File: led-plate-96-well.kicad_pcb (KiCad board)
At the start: 2 copper layers, 172.9 x 99.1 mm, 127 parts, among them J2 RAPC722X, U1 R-78E5.0-0.5, U2 A000053, U3 WST2N7002, U4 WST2N7002, U5 WST2N7002, U6 WST2N7002

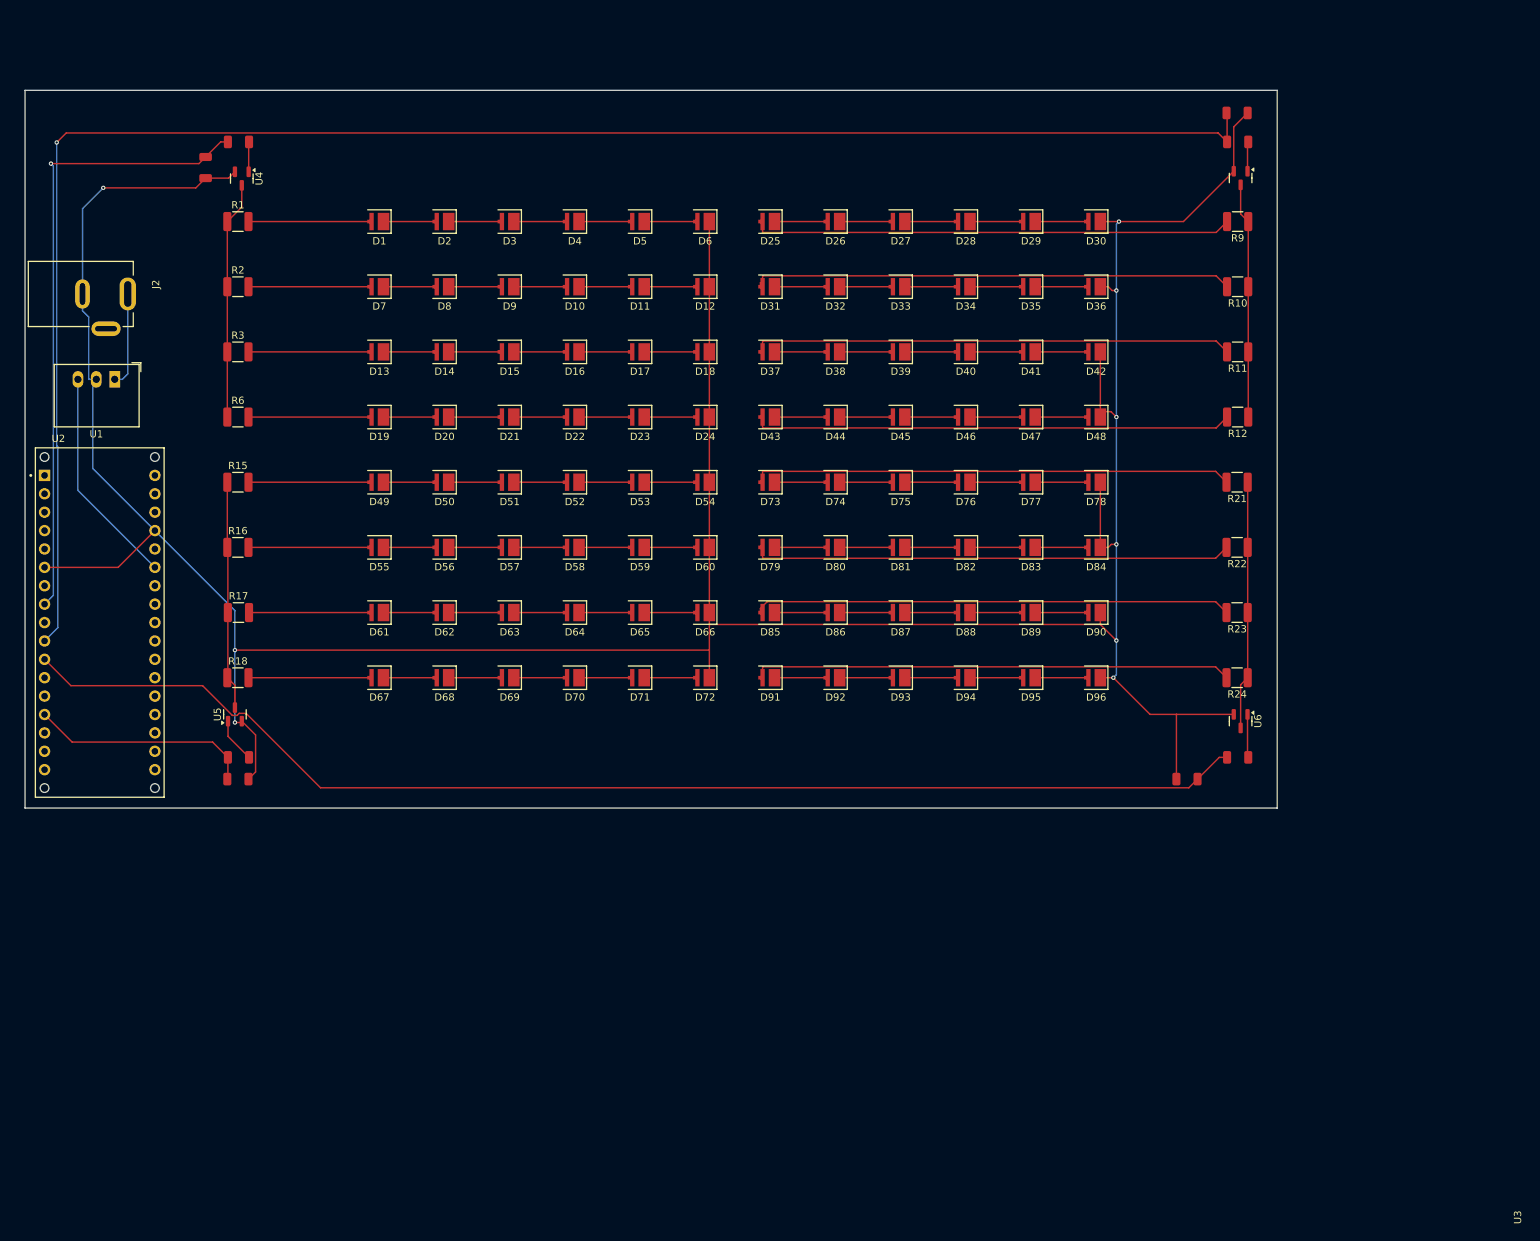
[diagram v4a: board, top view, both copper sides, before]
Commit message: drill holes, make more compact, re-route
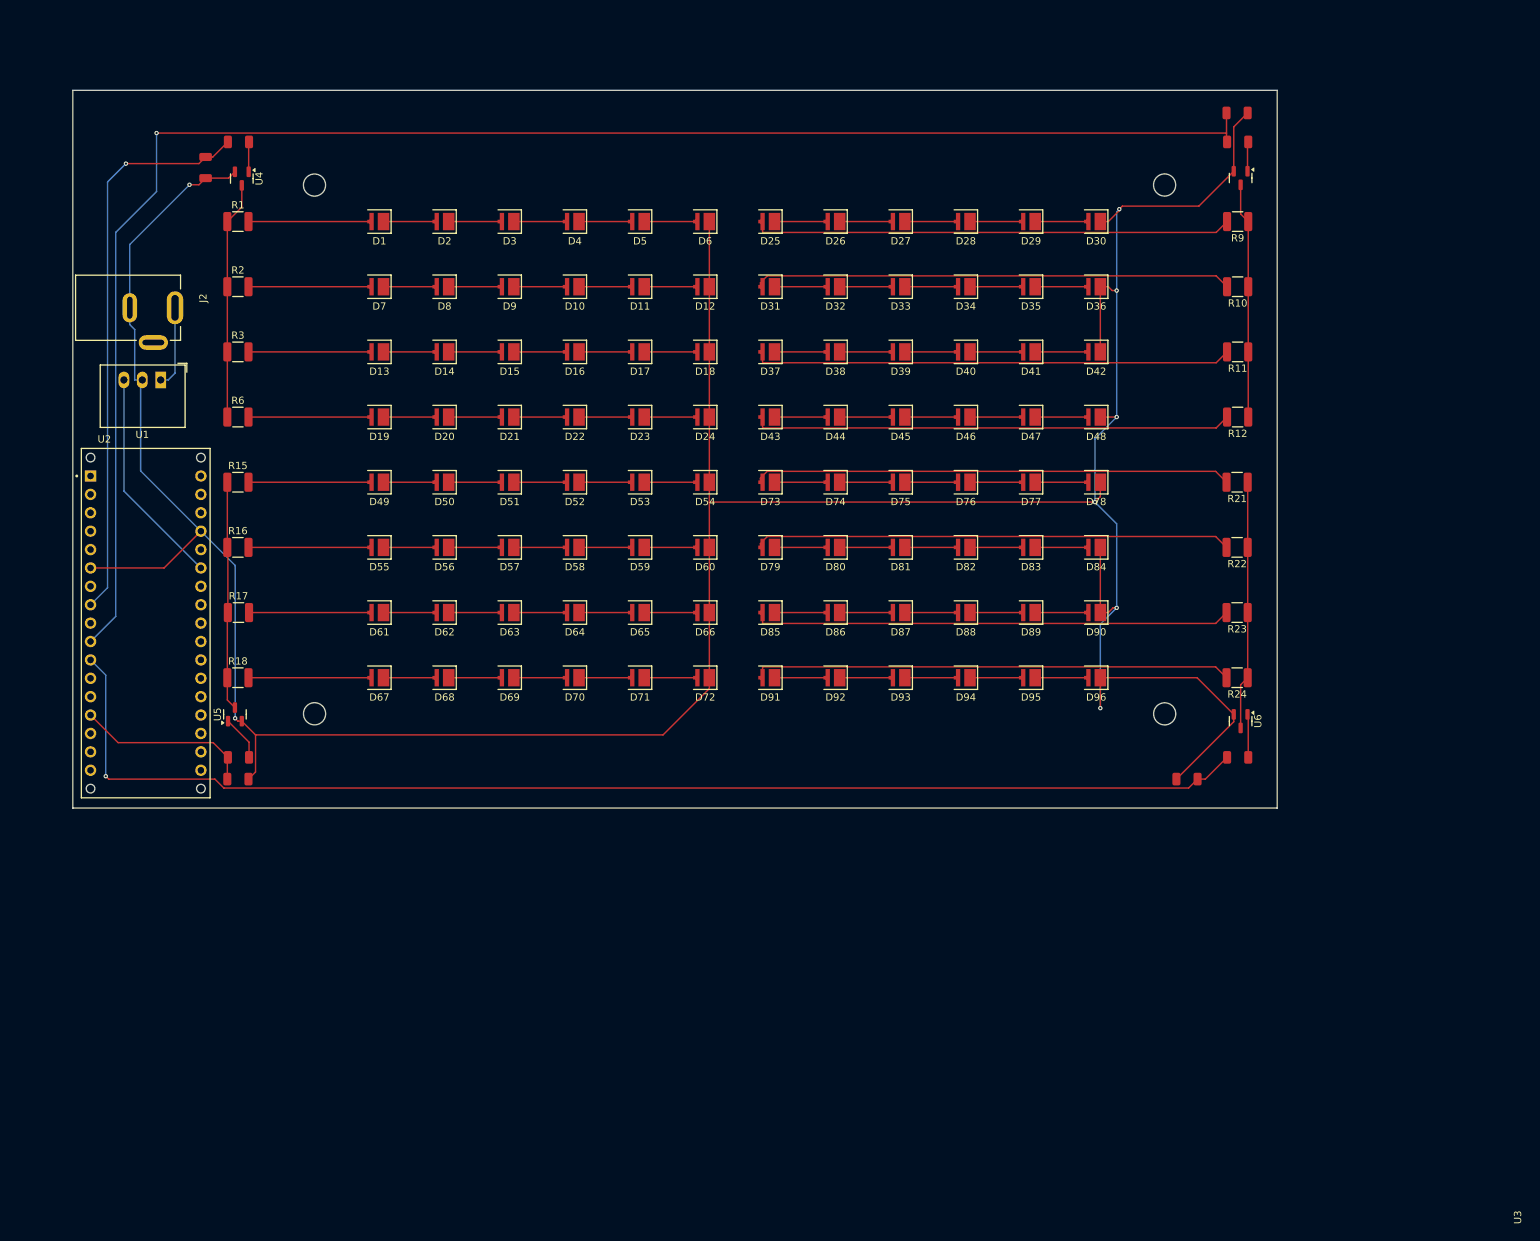
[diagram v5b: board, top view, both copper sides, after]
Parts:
- moved J2 6.80 mm to (91.1, 54.1)
- moved U1 6.35 mm to (95.4, 64.1)
- moved U2 6.35 mm to (93.3, 97.7)
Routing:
- net Net-(U2-5(PWM)): track 236.6 -> 225.8 mm
- net Net-(U2-3(PWM)/SCL): track 87.2 -> 78.3 mm
- net Net-(U2-9(PWM)/A9): track 30.8 -> 24.4 mm
- net GND: track 466.8 -> 469.6 mm, vias 9 -> 8
- net +24V: track 13.2 -> 11.4 mm
- net Net-(U2-6(PWM)/A7): track 172.6 -> 174.2 mm, vias 0 -> 1
- net Net-(U5-D): track 32.3 -> 31.6 mm
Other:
- board size 172.9 x 99.1 mm -> 166.3 x 99.1 mm

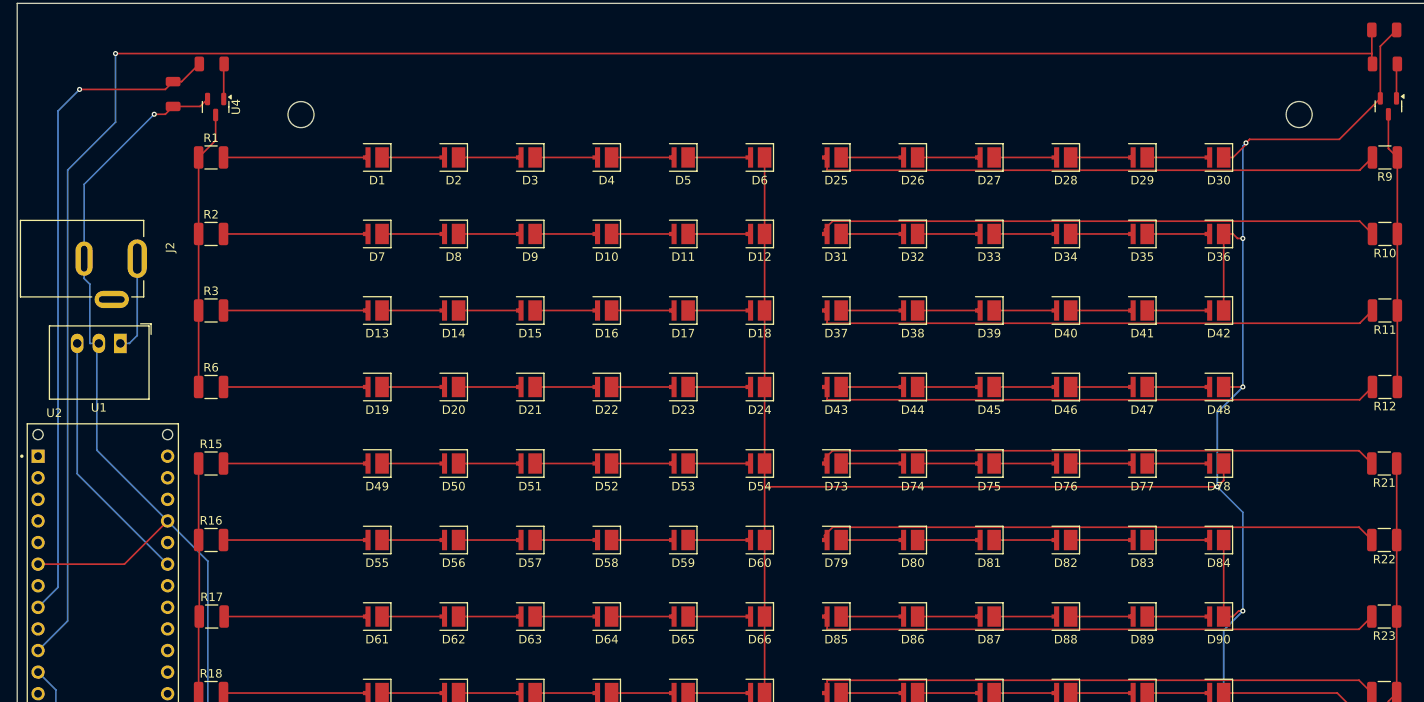
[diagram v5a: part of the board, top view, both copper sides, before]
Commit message: remove right angle
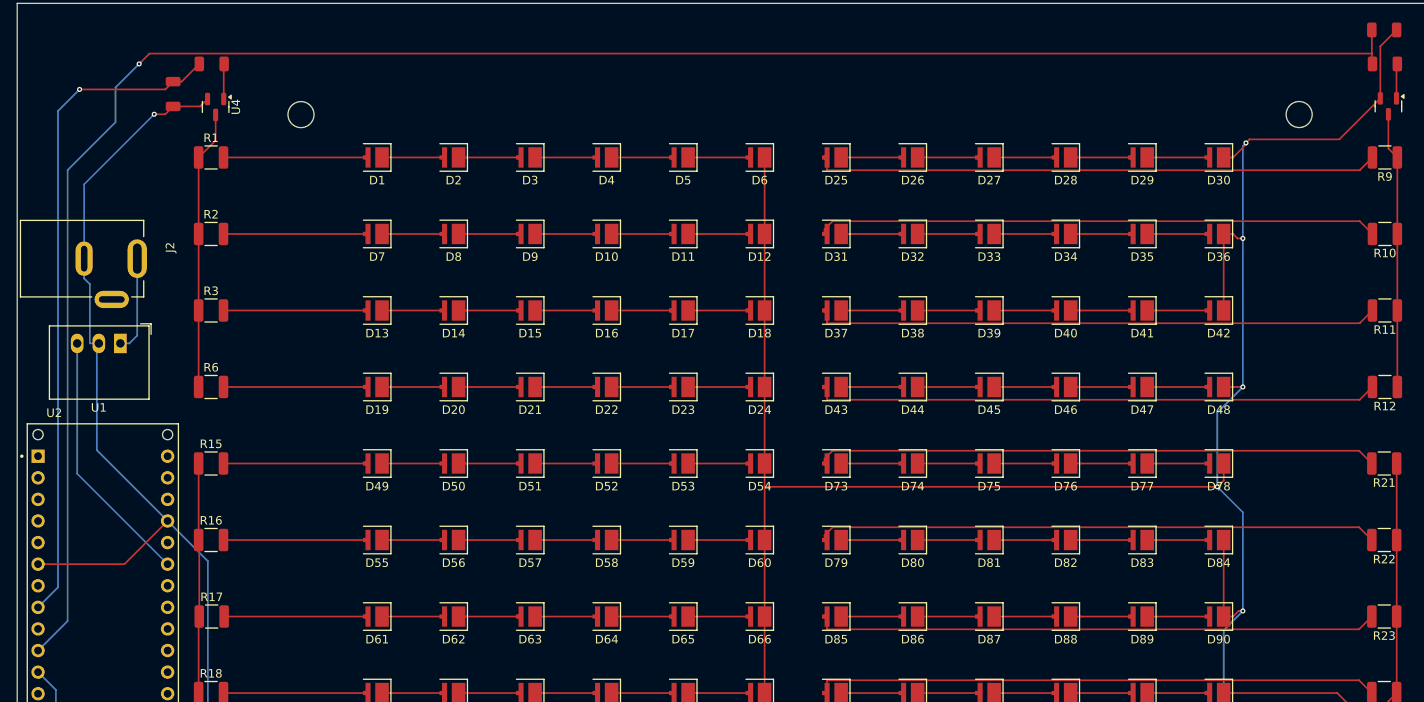
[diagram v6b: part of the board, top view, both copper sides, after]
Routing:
- net Net-(U2-5(PWM)): track 225.8 -> 223.5 mm
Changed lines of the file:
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@@
-	)
-	(segment
-		(start 242.57 29.989)
-		(end 94.7964 29.989)
-		(width 0.2)
-		(layer "F.Cu")
-		(net 129)
 	)
 	(segment
@@
 		(net 129)
 	)
+	(segment
+		(start 242.57 29.989)
+		(end 98.791 29.989)
+		(width 0.2)
+		(layer "F.Cu")
+		(net 129)
+	)
+	(segment
+		(start 98.791 29.989)
+		(end 97.57 31.21)
+		(width 0.2)
+		(layer "F.Cu")
+		(net 129)
+	)
 	(via
-		(at 94.7964 29.989)
+		(at 97.57 31.21)
 		(size 0.6)
 		(drill 0.3)
@@
 	)
 	(segment
+		(start 94.7964 38.0622)
+		(end 89.1617 43.6969)
+		(width 0.2)
+		(layer "B.Cu")
+		(net 129)
+	)
+	(segment
 		(start 89.1617 43.6969)
+		(end 89.1617 96.7283)
+		(width 0.2)
+		(layer "B.Cu")
+		(net 129)
+	)
+	(segment
+		(start 94.7964 33.9836)
 		(end 94.7964 38.0622)
 		(width 0.2)
@@
 	)
 	(segment
-		(start 94.7964 38.0622)
-		(end 94.7964 29.989)
+		(start 89.1617 96.7283)
+		(end 85.68 100.21)
 		(width 0.2)
 		(layer "B.Cu")
@@
 	)
 	(segment
-		(start 85.68 100.21)
-		(end 89.1617 96.7283)
+		(start 97.57 31.21)
+		(end 94.7964 33.9836)
 		(width 0.2)
 		(layer "B.Cu")
-		(net 129)
-	)
-	(segment
-		(start 89.1617 96.7283)
-		(end 89.1617 43.6969)
-		(width 0.2)
-		(layer "B.Cu")
